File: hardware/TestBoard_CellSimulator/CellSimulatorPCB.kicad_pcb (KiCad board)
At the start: 2 copper layers, 36.8 x 23.2 mm, 14 parts, among them J1 575-4, J11 Conn_01x07, J2 575-4

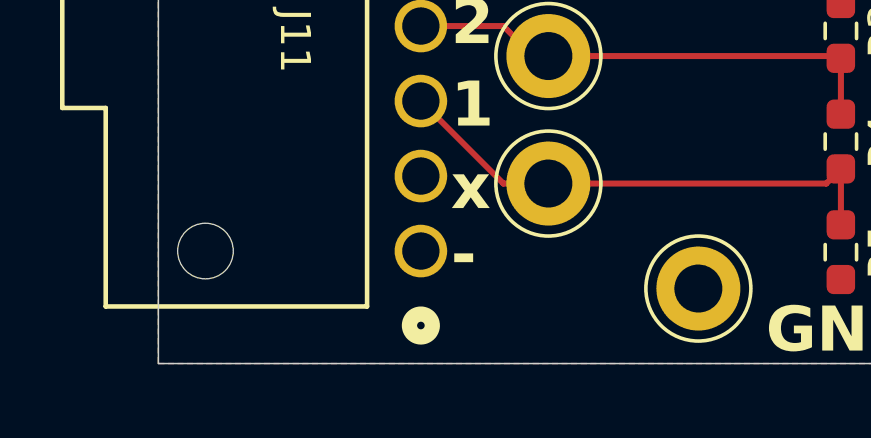
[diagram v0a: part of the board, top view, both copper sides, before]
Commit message: changed bild to sharepoint
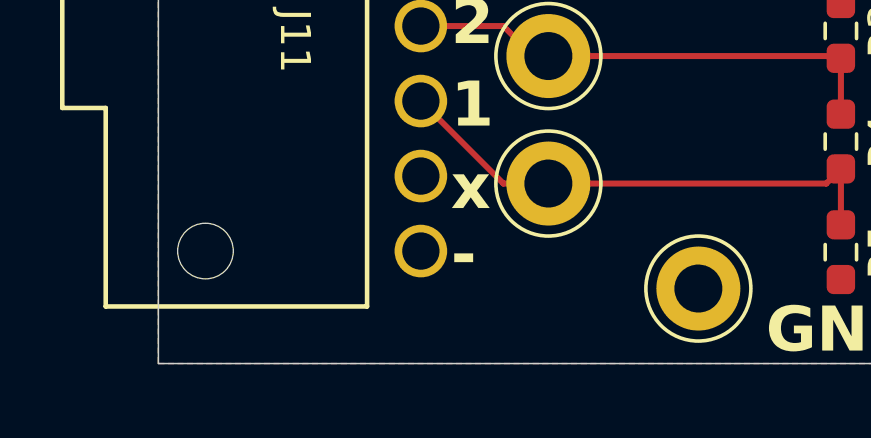
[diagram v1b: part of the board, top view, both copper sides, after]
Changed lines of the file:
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@@
 		)
 		(fp_circle
-			(center 2.4822 0)
-			(end 2.8632 0)
+			(center 1.4 0)
+			(end 1.4 0)
 			(stroke
 				(width 0.508)
@@
 		)
 		(fp_circle
-			(center 2.4822 0)
-			(end 2.8632 0)
+			(center 1.4 0)
+			(end 1.4 0)
 			(stroke
 				(width 0.508)
